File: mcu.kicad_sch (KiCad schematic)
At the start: 34 parts, among them J2 SWD, J3 SWC, U1 NRF52840-QIAA-R, Y1 FC-12M 32.7680KA-AC0, Y2 XRCGB32M000F1S2KR0

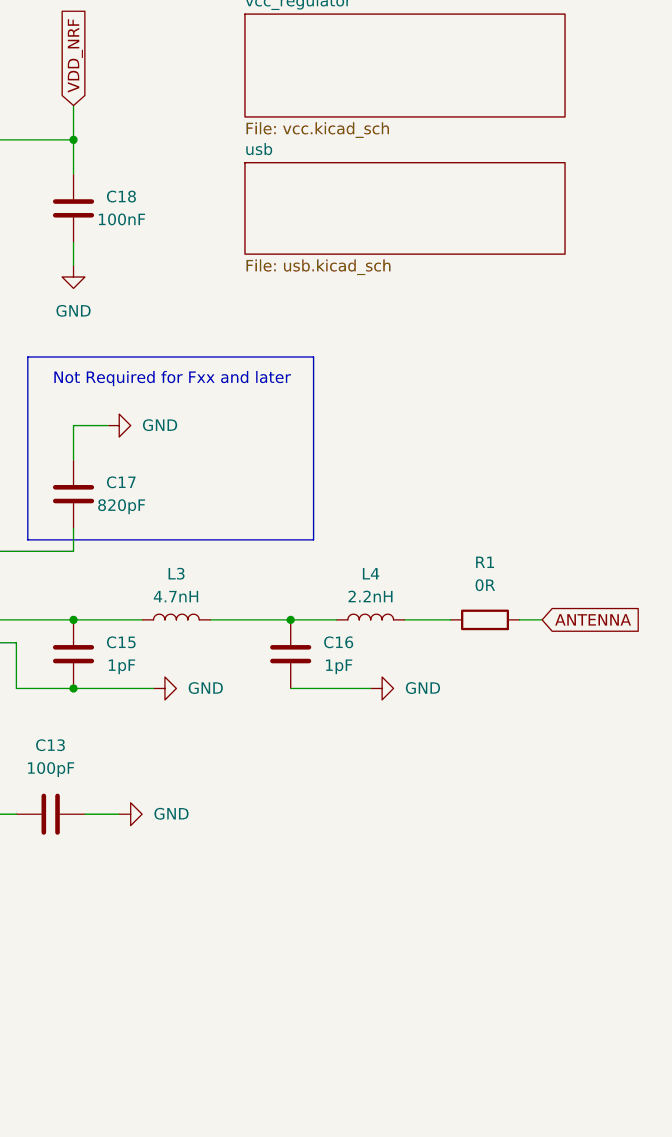
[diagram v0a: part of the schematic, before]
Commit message: Added PCB Test Layout
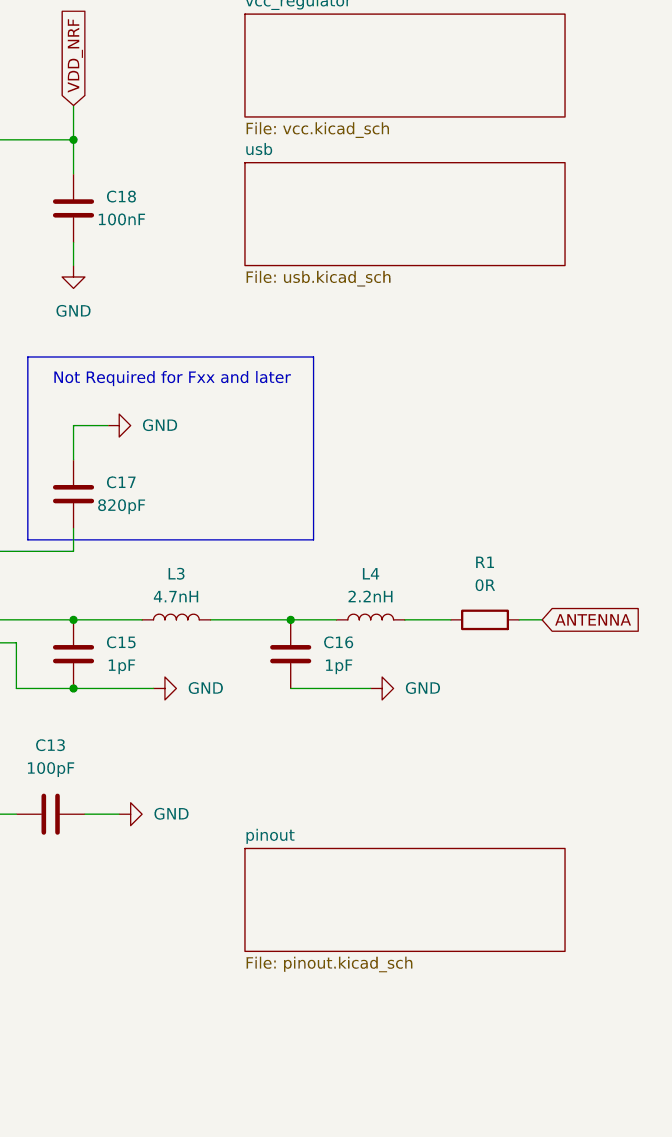
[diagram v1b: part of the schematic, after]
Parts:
- D3: footprint (none) -> LED_SMD:LED_0805_2012Metric
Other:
- added sheet pinout (pinout.kicad_sch)
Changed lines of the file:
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@@
 			)
 		)
-		(property "Footprint" ""
+		(property "Footprint" "LED_SMD:LED_0805_2012Metric"
 			(at 132.08 172.72 0)
 			(effects
@@
 	(sheet
 		(at 237.49 69.85)
-		(size 35.56 10.16)
+		(size 35.56 11.43)
 		(exclude_from_sim no)
 		(in_bom yes)
@@
 		)
 		(property "Sheetfile" "usb.kicad_sch"
-			(at 237.49 80.5946 0)
+			(at 237.49 81.8646 0)
 			(effects
 				(font
@@
 				)
 			)
+		)
+	)
+	(sheet
+		(at 237.49 146.05)
+		(size 35.56 11.43)
+		(exclude_from_sim no)
+		(in_bom yes)
+		(on_board yes)
+		(dnp no)
+		(fields_autoplaced yes)
+		(stroke
+			(width 0.1524)
+			(type solid)
+		)
+		(fill
+			(color 0 0 0 0.0000)
+		)
+		(property "Sheetname" "pinout"
+			(at 237.49 145.3384 0)
+			(effects
+				(font
+					(size 1.27 1.27)
+				)
+				(justify left bottom)
+			)
+		)
+		(property "Sheetfile" "pinout.kicad_sch"
+			(at 237.49 158.0646 0)
+			(effects
+				(font
+					(size 1.27 1.27)
+				)
+				(justify left top)
+			)
+		)
+		(instances
+			(project "Slim Keyboard"
+				(path "/5d65a0d4-45a3-4af0-996a-c0381d04499a/f42a8a8a-4a34-440a-8e58-9c442fe0d23e"
+					(page "8")
+				)
+			)

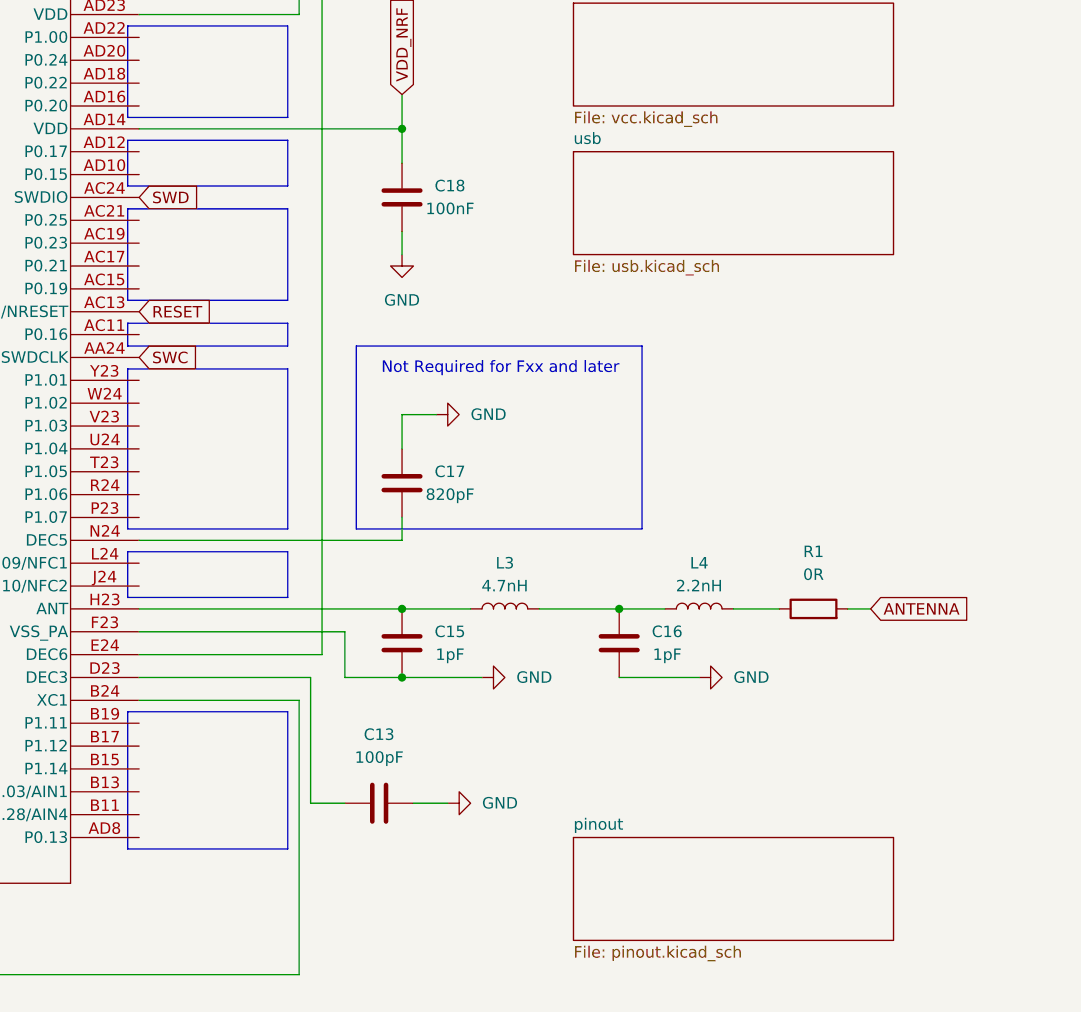
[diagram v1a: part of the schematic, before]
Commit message: Added test Antenna
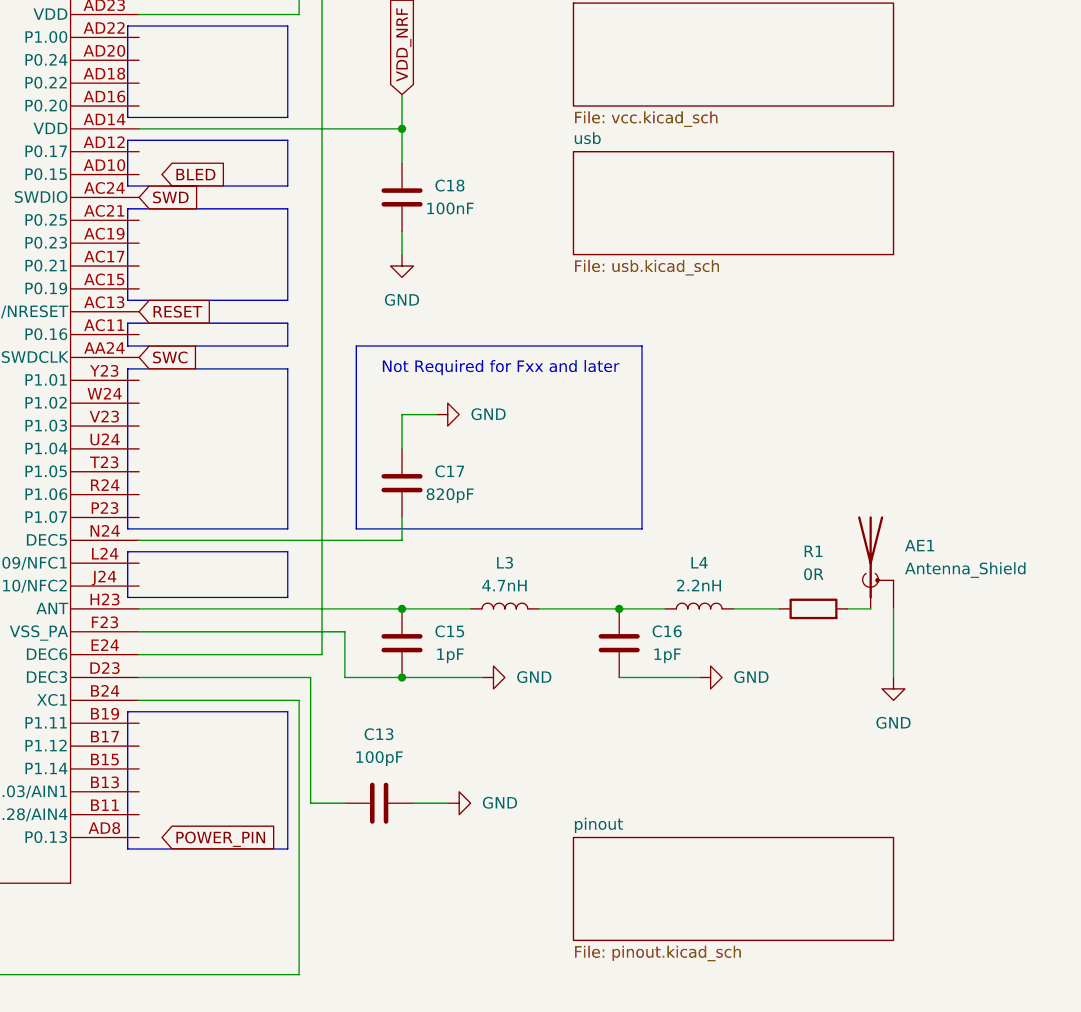
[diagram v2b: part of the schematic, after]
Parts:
- added AE1: Antenna_Shield, Antenna:2.4GHz F Antenna, symbol Device:Antenna_Shield
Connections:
- net GND: now also AE1.2 (Shield)
- net ANTENNA: no longer names the net of R1.2
- net ANTENNA: now also AE1.1 (A)
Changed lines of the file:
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@@
 	(wire
 		(pts
+			(xy 273.05 120.65) (xy 273.05 128.27)
+		)
+		(stroke
+			(width 0)
+			(type default)
+		)
+	)
+	(wire
+		(pts
 			(xy 87.63 105.41) (xy 87.63 128.27)
 		)
@@
 		)
 	)
-	(global_label "ANTENNA"
+	(global_label "SWD"
 		(shape input)
-		(at 270.51 120.65 0)
+		(at 123.19 182.88 180)
 		(fields_autoplaced yes)
 		(effects
@@
 				(size 1.27 1.27)
 			)
-			(justify left)
+			(justify right)
 		)
 		(property "Intersheetrefs" "${INTERSHEET_REFS}"
-			(at 281.7805 120.65 0)
+			(at 116.2739 182.88 0)
 			(effects
 				(font
 					(size 1.27 1.27)
 				)
-				(justify left)
+				(justify right)
 				(hide yes)
 			)
 		)
 	)
-	(global_label "SWD"
+	(global_label "VDD_NRF"
 		(shape input)
-		(at 123.19 182.88 180)
+		(at 38.1 120.65 90)
 		(fields_autoplaced yes)
 		(effects
@@
 				(size 1.27 1.27)
 			)
-			(justify right)
+			(justify left)
 		)
 		(property "Intersheetrefs" "${INTERSHEET_REFS}"
-			(at 116.2739 182.88 0)
+			(at 38.1 109.3795 90)
 			(effects
 				(font
 					(size 1.27 1.27)
 				)
-				(justify right)
+				(justify left)
 				(hide yes)
 			)
@@
 	(global_label "VDD_NRF"
 		(shape input)
-		(at 38.1 120.65 90)
+		(at 218.44 63.5 90)
 		(fields_autoplaced yes)
 		(effects
@@
 		)
 		(property "Intersheetrefs" "${INTERSHEET_REFS}"
-			(at 38.1 109.3795 90)
+			(at 218.44 52.2295 90)
 			(effects
 				(font
@@
 		)
 	)
-	(global_label "VDD_NRF"
+	(global_label "POWER_PIN"
 		(shape input)
-		(at 218.44 63.5 90)
+		(at 191.77 146.05 0)
 		(fields_autoplaced yes)
 		(effects
@@
 		)
 		(property "Intersheetrefs" "${INTERSHEET_REFS}"
-			(at 218.44 52.2295 90)
+			(at 205.399 146.05 0)
 			(effects
 				(font
@@
 		)
 	)
+	(global_label "BLED"
+		(shape input)
+		(at 191.77 72.39 0)
+		(fields_autoplaced yes)
+		(effects
+			(font
+				(size 1.27 1.27)
+			)
+			(justify left)
+		)
+		(property "Intersheetrefs" "${INTERSHEET_REFS}"
+			(at 199.4723 72.39 0)
+			(effects
+				(font
+					(size 1.27 1.27)
+				)
+				(justify left)
+				(hide yes)
+			)
+		)
+	)
 	(global_label "D-"
 		(shape input)
@@
 	)
 	(symbol
+		(lib_id "Device:Antenna_Shield")
+		(at 270.51 115.57 0)
+		(unit 1)
+		(exclude_from_sim no)
+		(in_bom yes)
+		(on_board yes)
+		(dnp no)
+		(fields_autoplaced yes)
+		(property "Reference" "AE1"
+			(at 274.32 113.6649 0)
+			(effects
+				(font
+					(size 1.27 1.27)
+				)
+				(justify left)
+			)
+		)
+		(property "Value" "Antenna_Shield"
+			(at 274.32 116.2049 0)
+			(effects
+				(font
+					(size 1.27 1.27)
+				)
+				(justify left)
+			)
+		)
+		(property "Footprint" "Antenna:2.4GHz F Antenna"
+			(at 270.51 113.03 0)
+			(effects
+				(font
+					(size 1.27 1.27)
+				)
+				(hide yes)
+			)
+		)
+		(property "Datasheet" "~"
+			(at 270.51 113.03 0)
+			(effects
+				(font
+					(size 1.27 1.27)
+				)
+				(hide yes)
+			)
+		)
+		(property "Description" "Antenna with extra pin for shielding"
+			(at 270.51 115.57 0)
+			(effects
+				(font
+					(size 1.27 1.27)
+				)
+				(hide yes)
+			)
+		)
+		(pin "2"
+		)
+		(pin "1"
+		)
+		(instances
+			(project ""
+				(path "/5d65a0d4-45a3-4af0-996a-c0381d04499a/f42a8a8a-4a34-440a-8e58-9c442fe0d23e"
+					(reference "AE1")
+					(unit 1)
+				)
+			)
+		)
+	)
+	(symbol
 		(lib_id "power:GND")
 		(at 102.87 148.59 0)
@@
 					(unit 1)
 				)
+			)
+		)
+	)
+	(symbol
+		(lib_id "power:GND")
+		(at 273.05 128.27 0)
+		(unit 1)
+		(exclude_from_sim no)
+		(in_bom yes)
+		(on_board yes)
+		(dnp no)
+		(fields_autoplaced yes)
+		(property "Reference" "#PWR040"
+			(at 273.05 134.62 0)
+			(effects
+				(font
+					(size 1.27 1.27)
+				)
+				(hide yes)
+			)
+		)
+		(property "Value" "GND"
+			(at 273.05 133.35 0)
+			(effects
+				(font
+					(size 1.27 1.27)
+				)
+			)
+		)
+		(property "Footprint" ""
+			(at 273.05 128.27 0)
+			(effects
+				(font
+					(size 1.27 1.27)
+				)
+				(hide yes)
+			)
+		)
+		(property "Datasheet" ""
+			(at 273.05 128.27 0)
+			(effects
+				(font
+					(size 1.27 1.27)
+				)
+				(hide yes)
+			)
+		)
+		(property "Description" "Power symbol creates a global label with name \"GND\" , ground"
+			(at 273.05 128.27 0)
+			(effects
+				(font
+					(size 1.27 1.27)
+				)
+				(hide yes)
+			)
+		)
+		(pin "1"
+		)
+		(instances
+			(project ""
+				(path "/5d65a0d4-45a3-4af0-996a-c0381d04499a/f42a8a8a-4a34-440a-8e58-9c442fe0d23e"
+					(reference "#PWR040")
+					(unit 1)
+				)

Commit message: Started PCB design
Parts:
- C16: value 1pF -> 1.2pF
- D3: value BLUE -> IN-S85AT5B
- R9: value R -> 1k
- Y1: value FC-12M 32.7680KA-AC0 -> ECS-.327-9-34B-TR
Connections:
- net BLED: now also U1.AD10 (P0.15)
- net POWER_PIN: now also U1.AD8 (P0.13)
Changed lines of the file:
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@@
 	(global_label "POWER_PIN"
 		(shape input)
-		(at 191.77 146.05 0)
+		(at 189.23 146.05 0)
 		(fields_autoplaced yes)
 		(effects
@@
 		)
 		(property "Intersheetrefs" "${INTERSHEET_REFS}"
-			(at 205.399 146.05 0)
+			(at 202.859 146.05 0)
 			(effects
 				(font
@@
 	(global_label "BLED"
 		(shape input)
-		(at 191.77 72.39 0)
+		(at 189.23 72.39 0)
 		(fields_autoplaced yes)
 		(effects
@@
 		)
 		(property "Intersheetrefs" "${INTERSHEET_REFS}"
-			(at 199.4723 72.39 0)
+			(at 196.9323 72.39 0)
 			(effects
 				(font
@@
 			)
 		)
-		(property "Value" "FC-12M 32.7680KA-AC0"
+		(property "Value" "ECS-.327-9-34B-TR"
 			(at 51.562 54.61 90)
 			(effects
@@
 			)
 		)
-		(property "Datasheet" "https://support.epson.biz/td/api/doc_check.php?dl=brief_FC-12M&lang=en"
+		(property "Datasheet" "https://ecsxtal.com/store/pdf/ecx-31b.pdf"
 			(at 58.42 58.42 0)
 			(effects
@@
 			)
 		)
-		(property "Description" "Unpolarized capacitor NP0"
+		(property "Description" "Unpolarized capacitor NP0 +-2"
 			(at 50.8 182.88 0)
 			(effects
@@
 			)
 		)
-		(property "Value" "R"
+		(property "Value" "1k"
 			(at 144.78 168.91 90)
 			(effects
@@
 			)
 		)
-		(property "Description" "Unpolarized capacitor NP0"
+		(property "Description" "Unpolarized capacitor NP0 +-2"
 			(at 48.26 49.53 0)
 			(effects
@@
 			)
 		)
-		(property "Description" "Unpolarized capacitor NP0"
+		(property "Description" "Unpolarized capacitor NP0 +-2"
 			(at 50.8 163.83 0)
 			(effects
@@
 			)
 		)
-		(property "Value" "BLUE"
+		(property "Value" "IN-S85AT5B"
 			(at 133.6675 167.64 0)
 			(effects
@@
 			)
 		)
-		(property "Datasheet" "~"
+		(property "Datasheet" "https://www.inolux-corp.com/datasheet/SMDLED/Mono%20Color%20Top%20View/IN-S85AT%20Series_V1.1.pdf"
 			(at 132.08 172.72 0)
 			(effects
@@
 			)
 		)
-		(property "Description" "Light emitting diode"
+		(property "Description" "Blue Light emitting diode"
 			(at 132.08 172.72 0)
 			(effects
@@
 			)
 		)
-		(property "Value" "1pF"
+		(property "Value" "1.2pF"
 			(at 247.904 125.73 0)
 			(effects
@@
 			)
 		)
-		(property "Description" "Unpolarized capacitor XR7"
+		(property "Description" "Unpolarized capacitor X7R"
 			(at 71.12 142.24 0)
 			(effects
@@
 			)
 		)
-		(property "Description" "Unpolarized capacitor NP0"
+		(property "Description" "Unpolarized capacitor NP0 +-2"
 			(at 48.26 68.58 0)
 			(effects

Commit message: Changed Pinout
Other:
- added sheet alt_LEDs (alt_leds.kicad_sch)
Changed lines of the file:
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@@
+		)
+	)
+	(sheet
+		(at 19.05 17.78)
+		(size 38.1 11.43)
+		(exclude_from_sim no)
+		(in_bom yes)
+		(on_board yes)
+		(dnp no)
+		(fields_autoplaced yes)
+		(stroke
+			(width 0.1524)
+			(type solid)
+		)
+		(fill
+			(color 0 0 0 0.0000)
+		)
+		(property "Sheetname" "alt_LEDs"
+			(at 19.05 17.0684 0)
+			(effects
+				(font
+					(size 1.27 1.27)
+				)
+				(justify left bottom)
+			)
+		)
+		(property "Sheetfile" "alt_leds.kicad_sch"
+			(at 19.05 29.7946 0)
+			(effects
+				(font
+					(size 1.27 1.27)
+				)
+				(justify left top)
+			)
+		)
+		(instances
+			(project "Slim Keyboard"
+				(path "/5d65a0d4-45a3-4af0-996a-c0381d04499a/f42a8a8a-4a34-440a-8e58-9c442fe0d23e"
+					(page "9")
+				)
+			)
 		)
 	)
